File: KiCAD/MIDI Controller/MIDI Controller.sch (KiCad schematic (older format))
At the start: 51 parts, among them J1 2040002-1, J2 Power, J3 MIDI, J4 Prog Jumper, U1 ATmega328PB-AU, U10 AD5293, U11 6N138, U2 FT232RL, U3 AD5293, U4 AD5293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

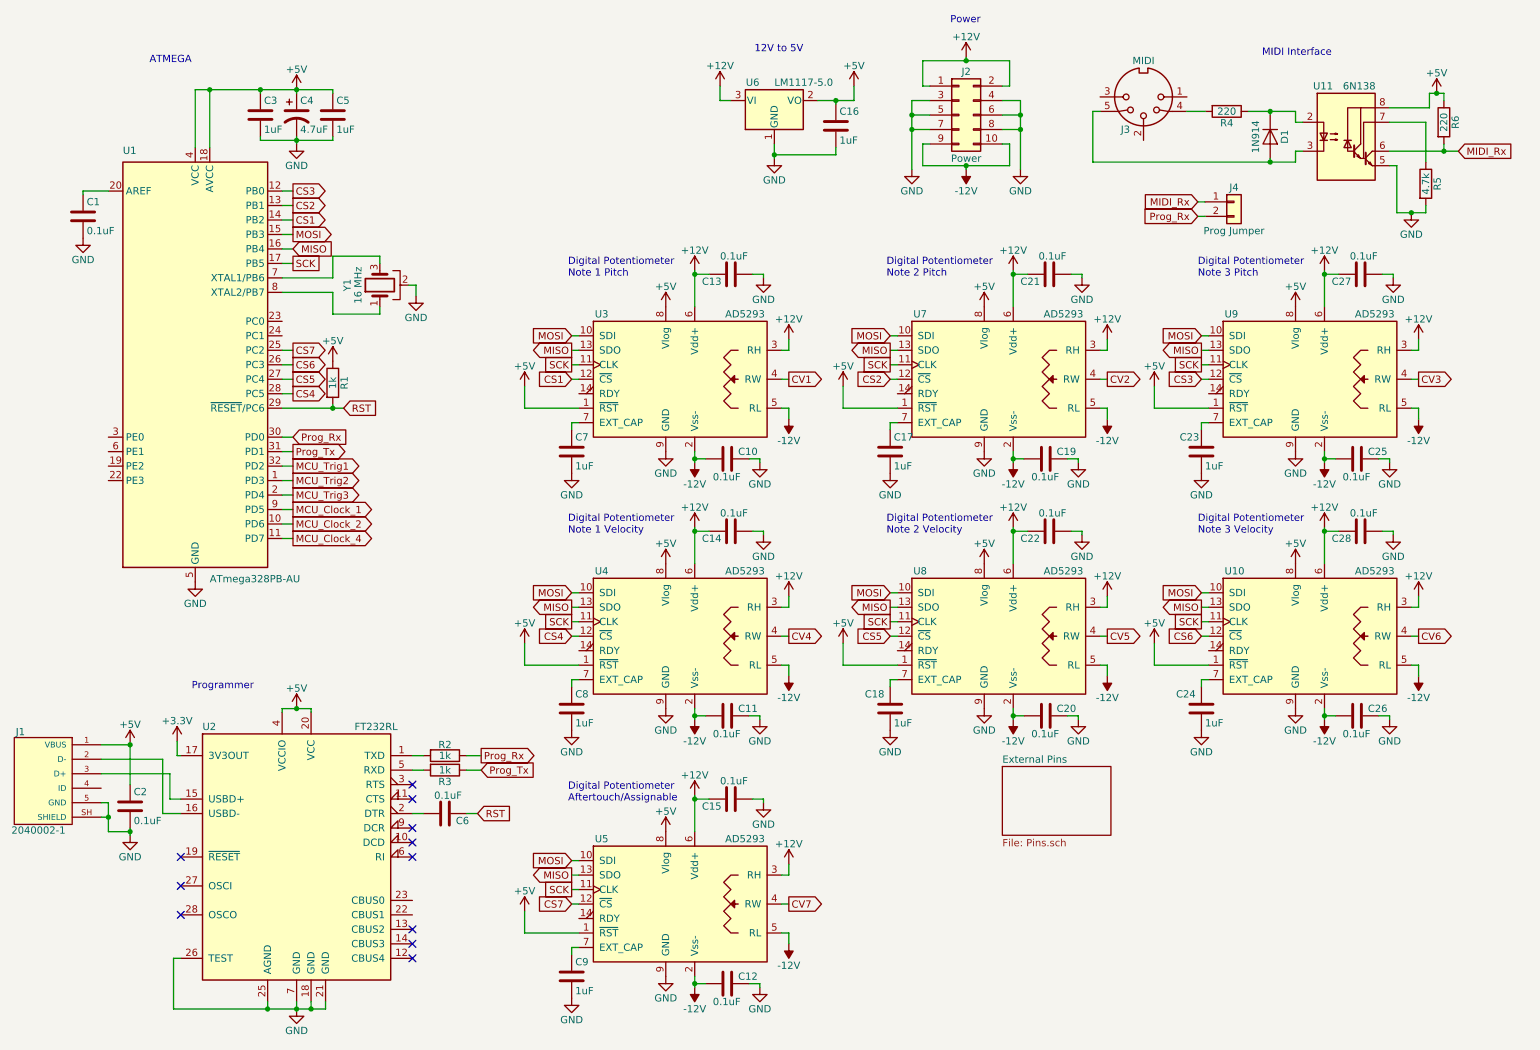
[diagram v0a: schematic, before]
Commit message: Added MIDI controller and PSU
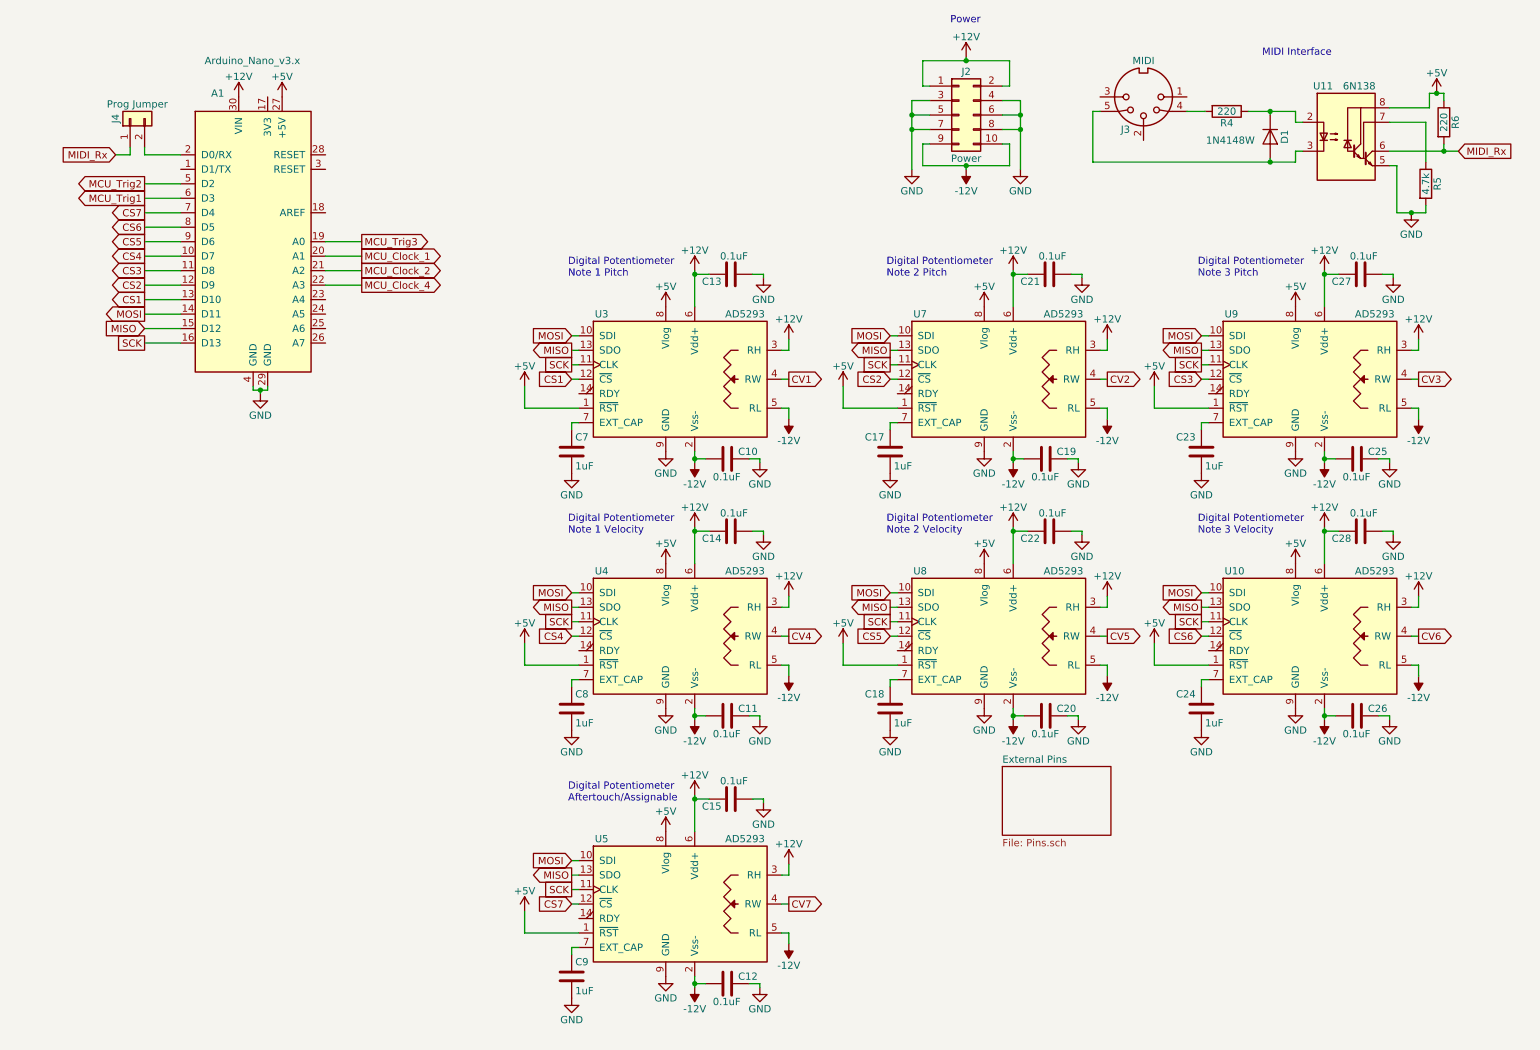
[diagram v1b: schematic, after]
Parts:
- removed C1, C2, C6: 0.1uF, Synth:C_1206, symbol Device:C
- removed C16, C3, C5: 1uF, Synth:C_1206, symbol Device:C
- removed C4: 4.7uF, Synth:C_1206, symbol Device:CP1
- removed J1: 2040002-1, Synth:2040002, symbol Synth:2040002-1
- removed R1, R2, R3: 1k, Synth:R_1206, symbol Device:R
- removed U1: ATmega328PB-AU, Package_QFP:TQFP-32_7x7mm_P0.8mm, symbol MCU_Microchip_ATmega:ATmega328PB-AU
- removed U2: FT232RL, Package_SO:SSOP-28_5.3x10.2mm_P0.65mm, symbol Interface_USB:FT232RL
- removed U6: LM1117-5.0, Package_TO_SOT_SMD:SOT-223-3_TabPin2, symbol Regulator_Linear:LM1117-5.0
- removed Y1: 16 MHz, Synth:Abracon_AWSCR_4.7x4.1mm, symbol Device:Crystal_GND2
- added A1: Arduino_Nano_v3.x, Module:Arduino_Nano, symbol MCU_Module:Arduino_Nano_v3.x
- C10, C11, C12, C13, C14, C15, C19, C20, C21, C22, C25, C26, C27, C28: Digikey Link (none) -> https://www.digikey.com/short/p4nr3m; Digikey PN (none) -> 720-1540-1-ND; Unit Price (none) -> 0.237
- C17, C18, C23, C24, C7, C8, C9: Digikey Link (none) -> https://www.digikey.com/short/p4nrpn; Digikey PN (none) -> 399-1254-1-ND; Unit Price (none) -> 0.23
- D1: value 1N914 -> 1N4148W; footprint Diode_THT:D_DO-35_SOD27_P7.62mm_Horizontal -> Synth:D_SOD-123; Digikey Link (none) -> https://www.digikey.com/short/p4nrz9; Digikey PN (none) -> 1N4148WTPMSCT-ND; Unit Price (none) -> 0.131
- J2: Digikey Link (none) -> https://www.digikey.com/short/p4nr84; Digikey PN (none) -> 609-3243-ND; Unit Price (none) -> 0.27
- J3: Digikey Link (none) -> https://www.digikey.com/short/p4nrpz; Digikey PN (none) -> CP-1250-ND; Unit Price (none) -> 2.99
- J4: Digikey Link (none) -> https://www.digikey.com/short/p4nrjv; Digikey PN (none) -> 732-5315-ND; Unit Price (none) -> 0.13
- R4, R6: Digikey Link (none) -> https://www.digikey.com/short/p4nrjp; Digikey PN (none) -> 311-220FRCT-ND; Unit Price (none) -> 0.10
- R5: Digikey Link (none) -> https://www.digikey.com/short/p4nr81; Digikey PN (none) -> A130181CT-ND; Unit Price (none) -> 0.10
- U10, U3, U4, U5, U7, U8, U9: Unit Price (none) -> 6.88
- U11: Digikey Link (none) -> https://www.digikey.com/short/p4nrj5; Digikey PN (none) -> 160-1795-ND; Unit Price (none) -> 0.81
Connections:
- net +12V: now also A1.30 (VIN)
- net +5V: now also A1.27 (+5V)
- net CS1: now also A1.13 (D10)
- net CS2: now also A1.12 (D9)
- net CS3: now also A1.11 (D8)
- net CS4: now also A1.10 (D7)
- net CS5: now also A1.9 (D6)
- net CS6: now also A1.8 (D5)
- net CS7: now also A1.7 (D4)
- net GND: now also A1.29 (GND), A1.4 (GND)
- net MCU_Clock_1: now also A1.20 (A1)
- net MCU_Clock_2: now also A1.21 (A2)
- net MCU_Clock_4: now also A1.22 (A3)
- net MCU_Trig1: now also A1.6 (D3)
- net MCU_Trig2: now also A1.5 (D2)
- net MCU_Trig3: now also A1.19 (A0)
- net MISO: now also A1.15 (D12)
- net MOSI: now also A1.14 (D11)
- net SCK: now also A1.16 (D13)
- net Prog_Rx: no longer names the net of J4.2 (Pin_2)
- net Prog_Rx: now also A1.2 (D0/RX)
- no-connect marks 11 -> 0
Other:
- note removed: "12V to 5V"
- note removed: "ATMEGA"
- note removed: "Programmer"
- moved on the sheet: J4
